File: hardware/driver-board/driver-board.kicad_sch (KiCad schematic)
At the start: 1 part, among them U3 STM32F103CBT6

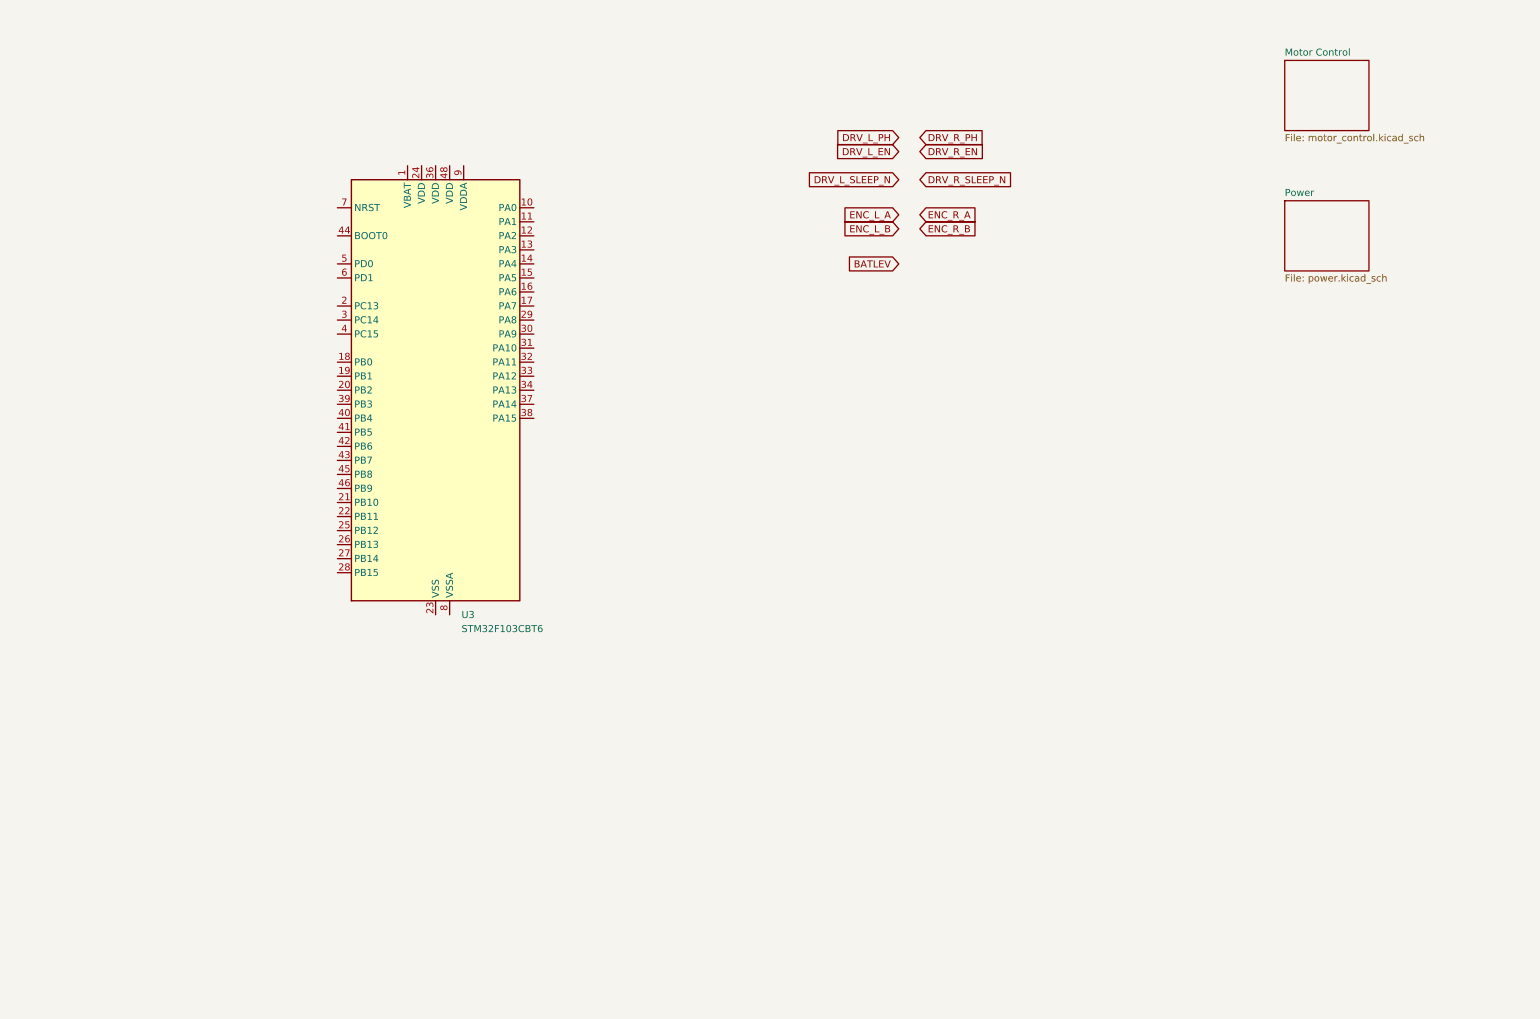
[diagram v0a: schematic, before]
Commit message: Checkpoint driver board schematic
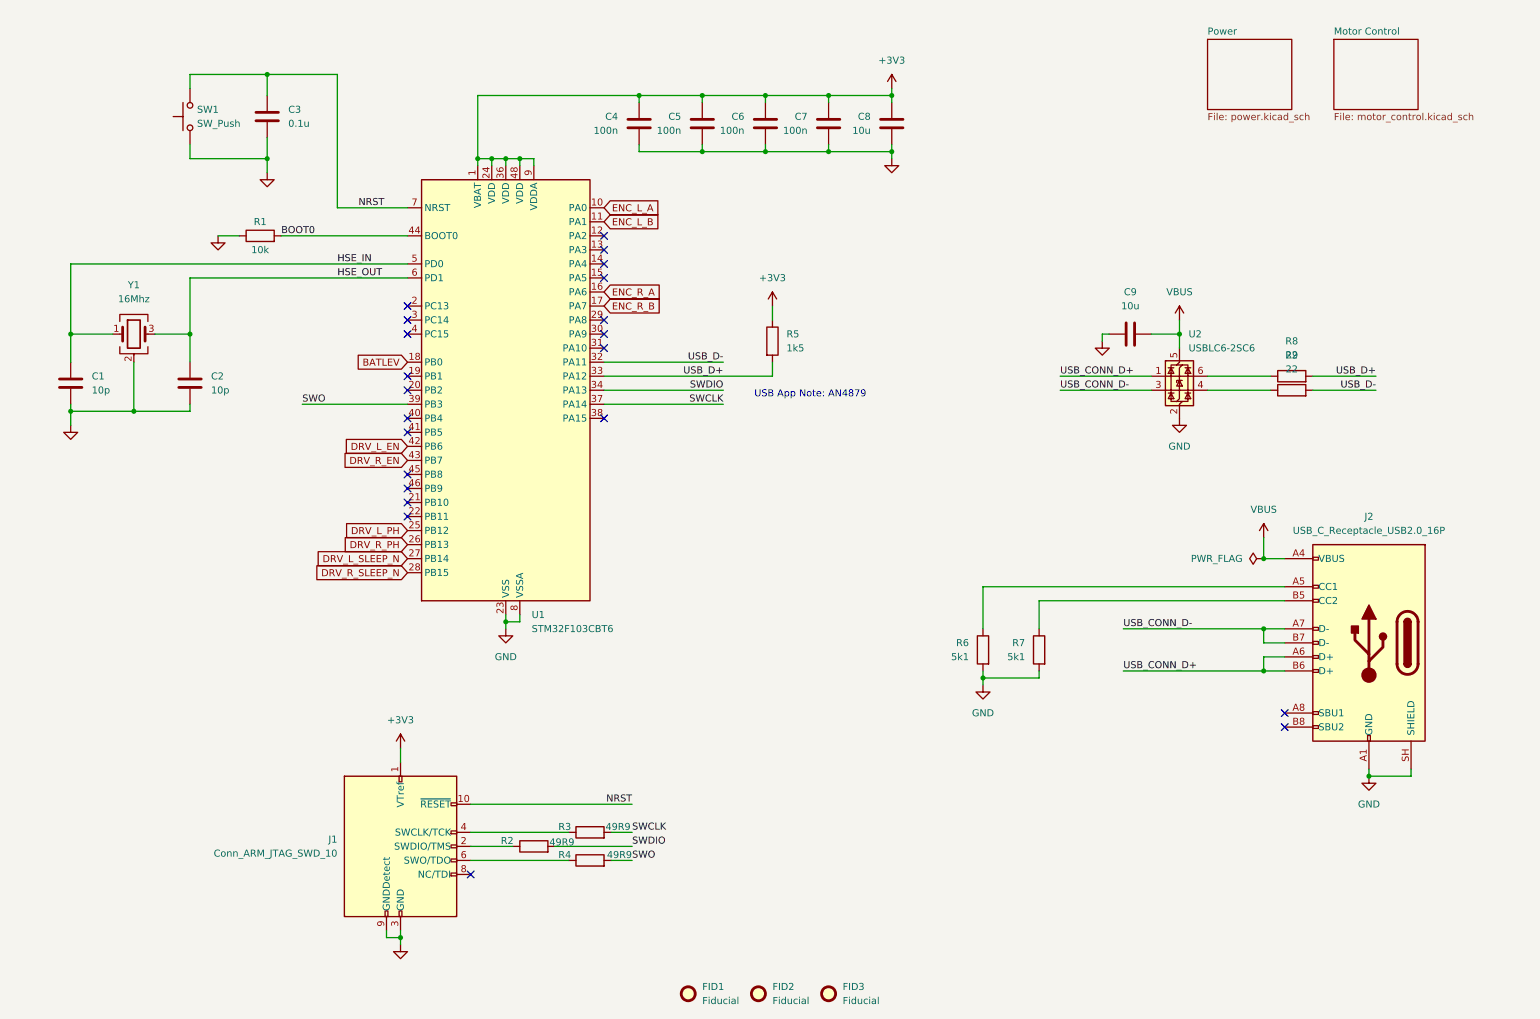
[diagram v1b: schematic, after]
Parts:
- added C1, C2: 10p, symbol Device:C
- added C3: 0.1u, Capacitor_SMD:C_0402_1005Metric, symbol Device:C
- added C4, C5, C6, C7: 100n, Capacitor_SMD:C_0603_1608Metric, symbol Device:C
- added C8: 10u, Capacitor_SMD:C_0402_1005Metric, symbol Device:C
- added C9: 10u, symbol Device:C
- added FID1, FID2, FID3: Fiducial, symbol Mechanical:Fiducial
- added J1: Conn_ARM_JTAG_SWD_10, Connector_PinHeader_1.27mm:PinHeader_2x05_P1.27mm_Vertical, symbol Connector:Conn_ARM_JTAG_SWD_10
- added J2: USB_C_Receptacle_USB2.0_16P, symbol Connector:USB_C_Receptacle_USB2.0_16P
- added R1: 10k, symbol Device:R
- added R2, R3, R4: 49R9, symbol Device:R
- added R5: 1k5, symbol Device:R
- added R6, R7: 5k1, symbol Device:R
- added R8, R9: 22, symbol Device:R
- added SW1: SW_Push, symbol Switch:SW_Push
- added U2: USBLC6-2SC6, Package_TO_SOT_SMD:SOT-23-6, symbol Power_Protection:USBLC6-2SC6
- added Y1: 16Mhz, symbol Device:Crystal_GND24
- renumbered U3 to U1
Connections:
- net BATLEV: now also U1.18 (PB0)
- net DRV_L_EN: now also U1.42 (PB6)
- net DRV_L_PH: now also U1.25 (PB12)
- net DRV_L_SLEEP_N: now also U1.27 (PB14)
- net DRV_R_EN: now also U1.43 (PB7)
- net DRV_R_PH: now also U1.26 (PB13)
- net DRV_R_SLEEP_N: now also U1.28 (PB15)
- net ENC_L_A: now also U1.10 (PA0)
- net ENC_L_B: now also U1.11 (PA1)
- net ENC_R_A: now also U1.16 (PA6)
- net ENC_R_B: now also U1.17 (PA7)
- net +3V3: now reaches U1.1 (VBAT)
- net +3V3: now also U1.24 (VDD), U1.36 (VDD), U1.48 (VDD), U1.9 (VDDA), C4.1, C5.1, C6.1, C7.1, C8.1, J1.1 (VTref), R5.1
- net GND: now reaches U1.23 (VSS), U1.35 (VSS), U1.47 (VSS)
- net GND: now also U1.8 (VSSA), C1.2, C2.2, C3.1, C4.2, C5.2, C6.2, C7.2, C8.2, C9.1, J1.3 (GND), J1.5 (GND), J1.9 (GNDDetect), J2.A1 (GND), J2.A12 (GND), J2.B1 (GND), J2.B12 (GND), J2.SH (SHIELD), R1.1, R6.2, R7.2, SW1.1, U2.2 (GND), Y1.2 (G), Y1.4 (G)
- net USB_D-: now reaches U1.32 (PA11)
- net USB_D-: now also R9.2
- net USB_D+: now reaches U1.33 (PA12)
- net USB_D+: now also R5.2, R8.2
- net SWDIO: now reaches U1.34 (PA13)
- net SWDIO: now also R2.2
- net SWCLK: now reaches U1.37 (PA14)
- net SWCLK: now also R3.2
- net SWO: now reaches U1.39 (PB3)
- net SWO: now also R4.2
- net BOOT0: now reaches U1.44 (BOOT0)
- net BOOT0: now also R1.2
- net HSE_IN: now reaches U1.5 (PD0)
- net HSE_IN: now also C1.1, Y1.1
- net HSE_OUT: now reaches U1.6 (PD1)
- net HSE_OUT: now also C2.1, Y1.3
- net NRST: now reaches U1.7 (NRST)
- net NRST: now also C3.2, J1.10 (~{RESET}), SW1.2
- new net: R8.1, U2.6 (I/O1)
- new net: R9.1, U2.4 (I/O2)
- new net: J1.4 (SWCLK/TCK), R3.1
- new net: J2.B5 (CC2), R7.1
- new net: J2.A5 (CC1), R6.1
- new net: J1.2 (SWDIO/TMS), R2.1
- new net: J1.6 (SWO/TDO), R4.1
- new net USB_CONN_D+: J2.A6 (D+), J2.B6 (D+), U2.1 (I/O1)
- new net USB_CONN_D-: J2.A7 (D-), J2.B7 (D-), U2.3 (I/O2)
- new net VBUS: C9.2, J2.A4 (VBUS), J2.A9 (VBUS), J2.B4 (VBUS), J2.B9 (VBUS), U2.5 (VBUS)
- no-connect marks 0 -> 22
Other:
- note added: "USB App Note: AN4879"
- moved on the sheet: U1

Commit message: Wrap up Rev A schematic pre-layout tasks
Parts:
- removed R2, R3, R4: 49R9, symbol Device:R
- C1, C2: footprint (none) -> Capacitor_SMD:C_0201_0603Metric; JLCPCB (none) -> C1634; JLCPCB Type (none) -> Basic
- C3: value 0.1u -> 100n; footprint Capacitor_SMD:C_0402_1005Metric -> Capacitor_SMD:C_0603_1608Metric; JLCPCB (none) -> C14663; JLCPCB Type (none) -> Basic
- C4, C5, C6, C7: JLCPCB Type (none) -> Basic
- C8: footprint Capacitor_SMD:C_0402_1005Metric -> Capacitor_SMD:C_1206_3216Metric; JLCPCB (none) -> C13585; JLCPCB Type (none) -> Basic
- C9: footprint (none) -> Capacitor_SMD:C_1206_3216Metric; JLCPCB (none) -> C13585; JLCPCB Type (none) -> Basic
- FID1, FID2, FID3: footprint (none) -> Fiducial:Fiducial_0.5mm_Mask1mm
- J2: footprint (none) -> Connector_USB:USB_C_Receptacle_G-Switch_GT-USB-7025; JLCPCB (none) -> C963213
- R1: footprint (none) -> Resistor_SMD:R_0603_1608Metric; JLCPCB (none) -> C25804; JLCPCB Type (none) -> Basic; MPN (none) -> 0603WAF1002T5E; Manufacturer (none) -> UNI-ROYAL
- R5: footprint (none) -> Resistor_SMD:R_0603_1608Metric; JLCPCB (none) -> C22843; JLCPCB Type (none) -> Basic
- R6, R7: footprint (none) -> Resistor_SMD:R_0603_1608Metric; JLCPCB (none) -> 0603; JLCPCB Type (none) -> Basic
- R8, R9: footprint (none) -> Resistor_SMD:R_0603_1608Metric; JLCPCB (none) -> C23345; JLCPCB Type (none) -> Basic
- SW1: footprint (none) -> Button_Switch_SMD:SW_SPST_TS-1088-xR020; JLCPCB (none) -> C720477; JLCPCB Type (none) -> Basic
- U2: JLCPCB (none) -> C7519
- Y1: footprint (none) -> Crystal:Crystal_SMD_3225-4Pin_3.2x2.5mm; JLCPCB (none) -> C13738; JLCPCB Type (none) -> Basic
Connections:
- net SWCLK: now also J1.4 (SWCLK/TCK)
- net SWDIO: now also J1.2 (SWDIO/TMS)
- net SWO: now also J1.6 (SWO/TDO)

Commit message: Add custom power entry footprints
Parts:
- added D2: STATUS, LED_SMD:LED_0603_1608Metric, symbol Device:LED
- added R21: 1k, Resistor_SMD:R_0603_1608Metric, symbol Device:R
- R6, R7: JLCPCB 0603 -> C23186
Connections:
- net GND: now also R21.2
- net at U1.2 (PC13): now also D2.2 (A)
- new net: D2.1 (K), R21.1
- no-connect marks 22 -> 21

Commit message: Complete Romi-compatible board placement and power switching
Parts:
- added H1, H2, H3, H4: MountingHole, CustomParts:MountingHole_2.3mm_2-56, symbol Mechanical:MountingHole
- J1: footprint Connector_PinHeader_1.27mm:PinHeader_2x05_P1.27mm_Vertical -> Connector_PinHeader_1.27mm:PinHeader_2x05_P1.27mm_Vertical_SMD; JLCPCB (none) -> C2932107

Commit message: Review and harden Rev A driver board
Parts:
- removed FID1, FID2, FID3: Fiducial, Fiducial:Fiducial_0.5mm_Mask1mm, symbol Mechanical:Fiducial
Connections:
- net +3V3: now also R21.1
- net GND: no longer R21.2
- net at U1.2 (PC13): now also D2.1 (K); no longer D2.2 (A)
- new net: D2.2 (A), R21.2
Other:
- moved on the sheet: D2, R21

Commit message: Refine driver board placement and capacitor footprints
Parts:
- C1, C2: footprint Capacitor_SMD:C_0201_0603Metric -> Capacitor_SMD:C_0402_1005Metric; JLCPCB C1634 -> C32949
- C3, C4, C5, C6, C7: footprint Capacitor_SMD:C_0603_1608Metric -> Capacitor_SMD:C_0402_1005Metric; JLCPCB C14663 -> C307331
- C8, C9: footprint Capacitor_SMD:C_1206_3216Metric -> Capacitor_SMD:C_0805_2012Metric; JLCPCB C13585 -> C15850
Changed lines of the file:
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@@
 			)
 		)
-		(property "Footprint" "Capacitor_SMD:C_0603_1608Metric"
+		(property "Footprint" "Capacitor_SMD:C_0402_1005Metric"
 			(at 138.7348 39.37 0)
 			(hide yes)
@@
 			)
 		)
-		(property "JLCPCB" "C14663"
+		(property "JLCPCB" "C307331"
 			(at 139.7 35.56 0)
 			(hide yes)
@@
 			)
 		)
-		(property "Footprint" "Capacitor_SMD:C_0201_0603Metric"
+		(property "Footprint" "Capacitor_SMD:C_0402_1005Metric"
 			(at 47.9552 86.36 0)
 			(hide yes)
@@
 			)
 		)
-		(property "JLCPCB" "C1634"
+		(property "JLCPCB" "C32949"
 			(at 46.99 82.55 0)
 			(hide yes)
@@
 			)
 		)
-		(property "Footprint" "Capacitor_SMD:C_0603_1608Metric"
+		(property "Footprint" "Capacitor_SMD:C_0402_1005Metric"
 			(at 161.5948 39.37 0)
 			(hide yes)
@@
 			)
 		)
-		(property "JLCPCB" "C14663"
+		(property "JLCPCB" "C307331"
 			(at 162.56 35.56 0)
 			(hide yes)
@@
 			)
 		)
-		(property "Footprint" "Capacitor_SMD:C_0603_1608Metric"
+		(property "Footprint" "Capacitor_SMD:C_0402_1005Metric"
 			(at 150.1648 39.37 0)
 			(hide yes)
@@
 			)
 		)
-		(property "JLCPCB" "C14663"
+		(property "JLCPCB" "C307331"
 			(at 151.13 35.56 0)
 			(hide yes)
@@
 			)
 		)
-		(property "Footprint" "Capacitor_SMD:C_0201_0603Metric"
+		(property "Footprint" "Capacitor_SMD:C_0402_1005Metric"
 			(at 26.3652 86.36 0)
 			(hide yes)
@@
 			)
 		)
-		(property "JLCPCB" "C1634"
+		(property "JLCPCB" "C32949"
 			(at 25.4 82.55 0)
 			(hide yes)
@@
 			)
 		)
-		(property "Footprint" "Capacitor_SMD:C_0603_1608Metric"
+		(property "Footprint" "Capacitor_SMD:C_0402_1005Metric"
 			(at 127.3048 39.37 0)
 			(hide yes)
@@
 			)
 		)
-		(property "JLCPCB" "C14663"
+		(property "JLCPCB" "C307331"
 			(at 128.27 35.56 0)
 			(hide yes)
@@
 			)
 		)
-		(property "Footprint" "Capacitor_SMD:C_0603_1608Metric"
+		(property "Footprint" "Capacitor_SMD:C_0402_1005Metric"
 			(at 59.9948 30.48 0)
 			(hide yes)
@@
 			)
 		)
-		(property "JLCPCB" "C14663"
+		(property "JLCPCB" "C307331"
 			(at 60.96 34.29 0)
 			(hide yes)
@@
 			)
 		)
-		(property "Footprint" "Capacitor_SMD:C_1206_3216Metric"
+		(property "Footprint" "Capacitor_SMD:C_0805_2012Metric"
 			(at 173.0248 39.37 0)
 			(hide yes)
@@
 			)
 		)
-		(property "JLCPCB" "C13585"
+		(property "JLCPCB" "C15850"
 			(at 173.99 35.56 0)
 			(hide yes)
@@
 			)
 		)
-		(property "Footprint" "Capacitor_SMD:C_1206_3216Metric"
+		(property "Footprint" "Capacitor_SMD:C_0805_2012Metric"
 			(at 220.98 72.6948 0)
 			(hide yes)
@@
 			)
 		)
-		(property "JLCPCB" "C13585"
+		(property "JLCPCB" "C15850"
 			(at 217.17 73.66 90)
 			(hide yes)

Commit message: Refine driver board placement and motor power checks
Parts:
- D2: footprint LED_SMD:LED_0603_1608Metric -> LED_SMD:LED_0805_2012Metric
- R1: footprint Resistor_SMD:R_0603_1608Metric -> Resistor_SMD:R_0402_1005Metric; JLCPCB C25804 -> C25744
- R5: footprint Resistor_SMD:R_0603_1608Metric -> Resistor_SMD:R_0402_1005Metric; JLCPCB C22843 -> (none)
- R6, R7: footprint Resistor_SMD:R_0603_1608Metric -> Resistor_SMD:R_0402_1005Metric; JLCPCB C23186 -> C25905
- R8, R9: footprint Resistor_SMD:R_0603_1608Metric -> Resistor_SMD:R_0402_1005Metric; JLCPCB C23345 -> C25092
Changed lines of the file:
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@@
 			)
 		)
-		(property "Footprint" "Resistor_SMD:R_0603_1608Metric"
+		(property "Footprint" "Resistor_SMD:R_0402_1005Metric"
 			(at 246.38 83.058 90)
 			(hide yes)
@@
 			)
 		)
-		(property "JLCPCB" "C23345"
+		(property "JLCPCB" "C25092"
 			(at 246.38 81.28 90)
 			(hide yes)
@@
 			)
 		)
-		(property "Footprint" "Resistor_SMD:R_0603_1608Metric"
+		(property "Footprint" "Resistor_SMD:R_0402_1005Metric"
 			(at 150.622 74.93 90)
 			(hide yes)
@@
 			)
 		)
-		(property "JLCPCB" "C22843"
+		(property "JLCPCB" ""
 			(at 152.4 74.93 0)
 			(hide yes)
@@
 			)
 		)
-		(property "Footprint" "Resistor_SMD:R_0603_1608Metric"
+		(property "Footprint" "Resistor_SMD:R_0402_1005Metric"
 			(at 246.38 85.598 90)
 			(hide yes)
@@
 			)
 		)
-		(property "JLCPCB" "C23345"
+		(property "JLCPCB" "C25092"
 			(at 246.38 83.82 90)
 			(hide yes)
@@
 			)
 		)
-		(property "Footprint" "Resistor_SMD:R_0603_1608Metric"
+		(property "Footprint" "Resistor_SMD:R_0402_1005Metric"
 			(at 202.438 130.81 90)
 			(hide yes)
@@
 			)
 		)
-		(property "JLCPCB" "C23186"
+		(property "JLCPCB" "C25905"
 			(at 200.66 130.81 0)
 			(hide yes)
@@
 			)
 		)
-		(property "Footprint" "Resistor_SMD:R_0603_1608Metric"
+		(property "Footprint" "Resistor_SMD:R_0402_1005Metric"
 			(at 59.69 57.658 90)
 			(hide yes)
@@
 			)
 		)
-		(property "JLCPCB" "C25804"
+		(property "JLCPCB" "C25744"
 			(at 59.69 55.88 0)
 			(hide yes)
@@
 			)
 		)
-		(property "Footprint" "LED_SMD:LED_0603_1608Metric"
+		(property "Footprint" "LED_SMD:LED_0805_2012Metric"
 			(at 49.53 119.38 0)
 			(hide yes)
@@
 			)
 		)
-		(property "Footprint" "Resistor_SMD:R_0603_1608Metric"
+		(property "Footprint" "Resistor_SMD:R_0402_1005Metric"
 			(at 192.278 130.81 90)
 			(hide yes)
@@
 			)
 		)
-		(property "JLCPCB" "C23186"
+		(property "JLCPCB" "C25905"
 			(at 190.5 130.81 0)
 			(hide yes)
